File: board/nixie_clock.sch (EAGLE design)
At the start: 43 parts, among them U1 AMS1117-5.0, U2 SN74141N

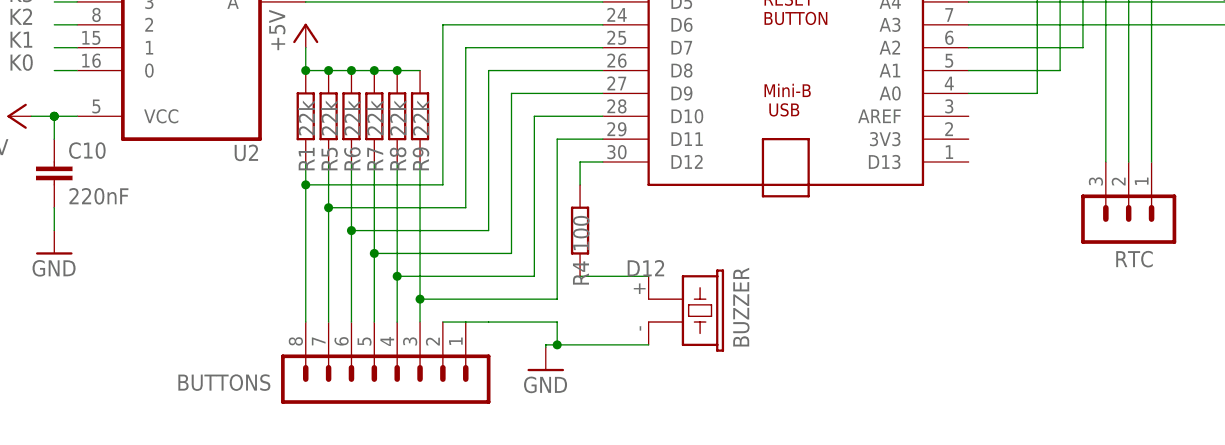
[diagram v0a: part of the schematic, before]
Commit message: added button to D13
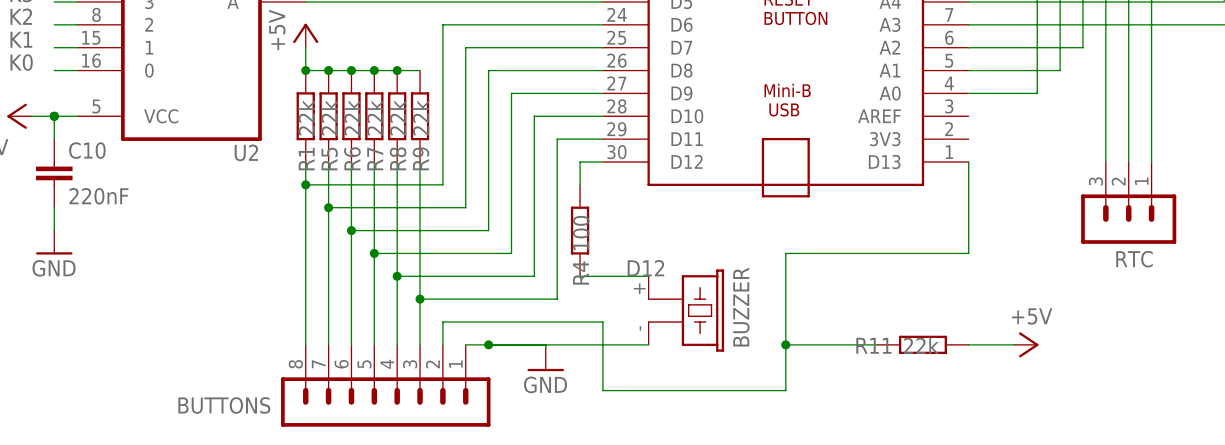
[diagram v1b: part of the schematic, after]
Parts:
- added R11: 22k, rcl:R-EU_0204/7
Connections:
- new net N$4: ARDUINO_NANO1.D13, BUTTONS.2, R11.2
- net +5V: now also R11.1
- net GND: no longer BUTTONS.2
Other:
- moved on the sheet: BUTTONS
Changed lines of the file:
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@@
 <part name="J1" library="con-jack" library_urn="urn:adsk.eagle:library:154" deviceset="DCJ0303" device="" package3d_urn="urn:adsk.eagle:package:7493/1"/>
 <part name="SHNT" library="switch" library_urn="urn:adsk.eagle:library:380" deviceset="320-916" device="" package3d_urn="urn:adsk.eagle:package:27678/1"/>
+<part name="R11" library="rcl" library_urn="urn:adsk.eagle:library:334" deviceset="R-EU_" device="0204/7" package3d_urn="urn:adsk.eagle:package:23498/2" value="22k"/>
+<part name="P+5" library="supply1" library_urn="urn:adsk.eagle:library:371" deviceset="+5V" device=""/>
 </parts>
 <sheets>
@@
 <frame x1="172.72" y1="127" x2="254" y2="177.8" columns="0" rows="1" layer="97" border-left="no" border-top="no" border-right="no" border-bottom="no"/>
 <text x="205.74" y="170.18" size="3.81" layer="97">200V Power supply</text>
-<frame x1="259.08" y1="53.34" x2="477.52" y2="215.9" columns="0" rows="0" layer="97" border-left="no" border-top="no" border-right="no" border-bottom="no"/>
+<frame x1="259.08" y1="45.72" x2="477.52" y2="208.28" columns="0" rows="0" layer="97" border-left="no" border-top="no" border-right="no" border-bottom="no"/>
 <text x="281.94" y="200.66" size="3.81" layer="97">Main circuit</text>
 <text x="45.72" y="114.3" size="3.81" layer="97">Nixie Tubes</text>
@@
 <attribute name="VALUE" x="309.118" y="88.138" size="1.778" layer="96" rot="R270"/>
 </instance>
-<instance part="BUTTONS" gate="1" x="307.34" y="55.88" smashed="yes" rot="R90">
-<attribute name="VALUE" x="320.04" y="54.61" size="1.778" layer="96" rot="R90"/>
-<attribute name="NAME" x="293.37" y="57.658" size="1.778" layer="95" rot="R180"/>
+<instance part="BUTTONS" gate="1" x="307.34" y="53.34" smashed="yes" rot="R90">
+<attribute name="VALUE" x="320.04" y="52.07" size="1.778" layer="96" rot="R90"/>
+<attribute name="NAME" x="293.37" y="55.118" size="1.778" layer="95" rot="R180"/>
 </instance>
 <instance part="BUZZER" gate="G$1" x="337.82" y="66.04" smashed="yes" rot="R270">
@@
 <attribute name="NAME" x="237.49" y="145.415" size="1.778" layer="95" rot="R90"/>
 <attribute name="VALUE" x="240.03" y="149.86" size="1.778" layer="96" rot="R90"/>
+</instance>
+<instance part="R11" gate="G$1" x="365.76" y="60.96" smashed="yes" rot="R180">
+<attribute name="NAME" x="362.458" y="61.7474" size="1.778" layer="95" rot="R180"/>
+<attribute name="VALUE" x="367.538" y="61.722" size="1.778" layer="96" rot="R180"/>
+</instance>
+<instance part="P+5" gate="1" x="378.46" y="60.96" smashed="yes" rot="R270">
+<attribute name="VALUE" x="375.412" y="63.246" size="1.778" layer="96"/>
 </instance>
 </instances>
@@
 <pinref part="BUZZER" gate="G$1" pin="2"/>
 <wire x1="323.85" y1="60.706" x2="323.85" y2="60.96" width="0.1524" layer="91"/>
-<wire x1="323.85" y1="60.96" x2="325.12" y2="60.96" width="0.1524" layer="91"/>
+<wire x1="323.85" y1="60.96" x2="317.5" y2="60.96" width="0.1524" layer="91"/>
 <pinref part="BUTTONS" gate="1" pin="1"/>
-<wire x1="325.12" y1="60.96" x2="335.28" y2="60.96" width="0.1524" layer="91"/>
-<wire x1="314.96" y1="63.5" x2="317.5" y2="63.5" width="0.1524" layer="91"/>
-<wire x1="317.5" y1="63.5" x2="325.12" y2="63.5" width="0.1524" layer="91"/>
-<wire x1="325.12" y1="63.5" x2="325.12" y2="60.96" width="0.1524" layer="91"/>
-<junction x="325.12" y="60.96"/>
-<pinref part="BUTTONS" gate="1" pin="2"/>
-<wire x1="312.42" y1="63.5" x2="314.96" y2="63.5" width="0.1524" layer="91"/>
+<wire x1="317.5" y1="60.96" x2="335.28" y2="60.96" width="0.1524" layer="91"/>
+<wire x1="314.96" y1="60.96" x2="317.5" y2="60.96" width="0.1524" layer="91"/>
+<junction x="317.5" y="60.96"/>
 </segment>
 <segment>
@@
 <pinref part="P+8" gate="1" pin="+5V"/>
 <wire x1="398.78" y1="116.84" x2="398.78" y2="121.92" width="0.1524" layer="91"/>
+</segment>
+<segment>
+<pinref part="P+5" gate="1" pin="+5V"/>
+<pinref part="R11" gate="G$1" pin="1"/>
+<wire x1="375.92" y1="60.96" x2="370.84" y2="60.96" width="0.1524" layer="91"/>
 </segment>
 </net>
@@
 <wire x1="309.88" y1="81.28" x2="309.88" y2="66.04" width="0.1524" layer="91"/>
 <pinref part="ARDUINO_NANO1" gate="G$1" pin="D11"/>
-<wire x1="309.88" y1="66.04" x2="309.88" y2="63.5" width="0.1524" layer="91"/>
+<wire x1="309.88" y1="66.04" x2="309.88" y2="60.96" width="0.1524" layer="91"/>
 <wire x1="330.2" y1="83.82" x2="325.12" y2="83.82" width="0.1524" layer="91"/>
 <wire x1="325.12" y1="83.82" x2="325.12" y2="66.04" width="0.1524" layer="91"/>
@@
 <wire x1="307.34" y1="81.28" x2="307.34" y2="68.58" width="0.1524" layer="91"/>
 <pinref part="ARDUINO_NANO1" gate="G$1" pin="D10"/>
-<wire x1="307.34" y1="68.58" x2="307.34" y2="63.5" width="0.1524" layer="91"/>
+<wire x1="307.34" y1="68.58" x2="307.34" y2="60.96" width="0.1524" layer="91"/>
 <wire x1="330.2" y1="86.36" x2="322.58" y2="86.36" width="0.1524" layer="91"/>
 <wire x1="322.58" y1="86.36" x2="322.58" y2="68.58" width="0.1524" layer="91"/>
@@
 <wire x1="304.8" y1="81.28" x2="304.8" y2="71.12" width="0.1524" layer="91"/>
 <pinref part="ARDUINO_NANO1" gate="G$1" pin="D9"/>
-<wire x1="304.8" y1="71.12" x2="304.8" y2="63.5" width="0.1524" layer="91"/>
+<wire x1="304.8" y1="71.12" x2="304.8" y2="60.96" width="0.1524" layer="91"/>
 <wire x1="330.2" y1="88.9" x2="320.04" y2="88.9" width="0.1524" layer="91"/>
 <wire x1="320.04" y1="88.9" x2="320.04" y2="71.12" width="0.1524" layer="91"/>
@@
 <wire x1="302.26" y1="81.28" x2="302.26" y2="73.66" width="0.1524" layer="91"/>
 <pinref part="ARDUINO_NANO1" gate="G$1" pin="D8"/>
-<wire x1="302.26" y1="73.66" x2="302.26" y2="63.5" width="0.1524" layer="91"/>
+<wire x1="302.26" y1="73.66" x2="302.26" y2="60.96" width="0.1524" layer="91"/>
 <wire x1="330.2" y1="91.44" x2="317.5" y2="91.44" width="0.1524" layer="91"/>
 <wire x1="317.5" y1="91.44" x2="317.5" y2="73.66" width="0.1524" layer="91"/>
@@
 <wire x1="299.72" y1="81.28" x2="299.72" y2="76.2" width="0.1524" layer="91"/>
 <pinref part="ARDUINO_NANO1" gate="G$1" pin="D7"/>
-<wire x1="299.72" y1="76.2" x2="299.72" y2="63.5" width="0.1524" layer="91"/>
+<wire x1="299.72" y1="76.2" x2="299.72" y2="60.96" width="0.1524" layer="91"/>
 <wire x1="330.2" y1="93.98" x2="314.96" y2="93.98" width="0.1524" layer="91"/>
 <wire x1="314.96" y1="93.98" x2="314.96" y2="76.2" width="0.1524" layer="91"/>
@@
 <wire x1="297.18" y1="81.28" x2="297.18" y2="78.74" width="0.1524" layer="91"/>
 <pinref part="ARDUINO_NANO1" gate="G$1" pin="D6"/>
-<wire x1="297.18" y1="78.74" x2="297.18" y2="63.5" width="0.1524" layer="91"/>
+<wire x1="297.18" y1="78.74" x2="297.18" y2="60.96" width="0.1524" layer="91"/>
 <wire x1="330.2" y1="96.52" x2="312.42" y2="96.52" width="0.1524" layer="91"/>
 <wire x1="312.42" y1="96.52" x2="312.42" y2="78.74" width="0.1524" layer="91"/>
@@
 </segment>
 </net>
+<net name="N$4" class="0">
+<segment>
+<pinref part="R11" gate="G$1" pin="2"/>
+<wire x1="360.68" y1="60.96" x2="350.52" y2="60.96" width="0.1524" layer="91"/>
+<wire x1="350.52" y1="60.96" x2="350.52" y2="55.88" width="0.1524" layer="91"/>
+<wire x1="350.52" y1="55.88" x2="330.2" y2="55.88" width="0.1524" layer="91"/>
+<wire x1="330.2" y1="55.88" x2="330.2" y2="63.5" width="0.1524" layer="91"/>
+<pinref part="BUTTONS" gate="1" pin="2"/>
+<wire x1="330.2" y1="63.5" x2="312.42" y2="63.5" width="0.1524" layer="91"/>
+<wire x1="312.42" y1="63.5" x2="312.42" y2="60.96" width="0.1524" layer="91"/>
+<pinref part="ARDUINO_NANO1" gate="G$1" pin="D13"/>
+<wire x1="370.84" y1="81.28" x2="370.84" y2="71.12" width="0.1524" layer="91"/>
+<wire x1="370.84" y1="71.12" x2="350.52" y2="71.12" width="0.1524" layer="91"/>
+<wire x1="350.52" y1="71.12" x2="350.52" y2="60.96" width="0.1524" layer="91"/>
+<junction x="350.52" y="60.96"/>
+</segment>
+</net>

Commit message: finalized board component layout
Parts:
- removed J1: (no value), con-jack:DCJ0303
- added INPUT: 22-23-2021, con-molex:22-23-2021
- SHNT: value (none) -> 22-23-2021; device switch:320-916 -> con-molex:22-23-2021
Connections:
- net +12V: now also SHNT-2.S; no longer SHNT.O, SHNT.S
- net GND: now also INPUT-2.S, SHNT-1.S; no longer J1.1, J1.2, SHNT.P
- net N$1: now also INPUT-1.S; no longer J1.3
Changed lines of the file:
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@@
 <part name="R10" library="rcl" library_urn="urn:adsk.eagle:library:334" deviceset="R-EU_" device="0204/7" package3d_urn="urn:adsk.eagle:package:23498/2" value="670"/>
 <part name="GND9" library="supply1" library_urn="urn:adsk.eagle:library:371" deviceset="GND" device=""/>
-<part name="J1" library="con-jack" library_urn="urn:adsk.eagle:library:154" deviceset="DCJ0303" device="" package3d_urn="urn:adsk.eagle:package:7493/1"/>
-<part name="SHNT" library="switch" library_urn="urn:adsk.eagle:library:380" deviceset="320-916" device="" package3d_urn="urn:adsk.eagle:package:27678/1"/>
 <part name="R11" library="rcl" library_urn="urn:adsk.eagle:library:334" deviceset="R-EU_" device="0204/7" package3d_urn="urn:adsk.eagle:package:23498/2" value="22k"/>
 <part name="P+5" library="supply1" library_urn="urn:adsk.eagle:library:371" deviceset="+5V" device=""/>
+<part name="SHNT" library="con-molex" library_urn="urn:adsk.eagle:library:165" deviceset="22-23-2021" device="" package3d_urn="urn:adsk.eagle:package:8078633/1"/>
+<part name="INPUT" library="con-molex" library_urn="urn:adsk.eagle:library:165" deviceset="22-23-2021" device="" package3d_urn="urn:adsk.eagle:package:8078633/1"/>
 </parts>
 <sheets>
@@
 <attribute name="VALUE" x="269.24" y="157.48" size="1.778" layer="96"/>
 </instance>
-<instance part="J1" gate="G$1" x="45.72" y="167.64" smashed="yes">
-<attribute name="NAME" x="43.18" y="171.45" size="1.778" layer="95"/>
-<attribute name="VALUE" x="43.18" y="161.29" size="1.778" layer="96"/>
-</instance>
-<instance part="SHNT" gate="1" x="243.84" y="147.32" smashed="yes">
-<attribute name="NAME" x="237.49" y="145.415" size="1.778" layer="95" rot="R90"/>
-<attribute name="VALUE" x="240.03" y="149.86" size="1.778" layer="96" rot="R90"/>
-</instance>
 <instance part="R11" gate="G$1" x="365.76" y="60.96" smashed="yes" rot="R180">
 <attribute name="NAME" x="362.458" y="61.7474" size="1.778" layer="95" rot="R180"/>
@@
 <instance part="P+5" gate="1" x="378.46" y="60.96" smashed="yes" rot="R270">
 <attribute name="VALUE" x="375.412" y="63.246" size="1.778" layer="96"/>
+</instance>
+<instance part="SHNT" gate="-1" x="243.84" y="142.24" smashed="yes">
+<attribute name="NAME" x="246.38" y="141.478" size="1.524" layer="95"/>
+</instance>
+<instance part="SHNT" gate="-2" x="243.84" y="144.78" smashed="yes">
+<attribute name="NAME" x="246.38" y="144.018" size="1.524" layer="95"/>
+</instance>
+<instance part="INPUT" gate="-1" x="48.26" y="167.64" smashed="yes" rot="R180">
+<attribute name="NAME" x="50.8" y="170.942" size="1.524" layer="95" rot="R180"/>
+</instance>
+<instance part="INPUT" gate="-2" x="48.26" y="165.1" smashed="yes" rot="R180">
+<attribute name="NAME" x="50.8" y="163.322" size="1.524" layer="95" rot="R180"/>
 </instance>
 </instances>
@@
 <segment>
 <pinref part="GND1" gate="1" pin="GND"/>
-<wire x1="58.42" y1="142.24" x2="73.66" y2="142.24" width="0.1524" layer="91"/>
+<wire x1="55.88" y1="142.24" x2="73.66" y2="142.24" width="0.1524" layer="91"/>
 <pinref part="C1" gate="G$1" pin="2"/>
 <wire x1="73.66" y1="142.24" x2="91.44" y2="142.24" width="0.1524" layer="91"/>
@@
 <wire x1="101.6" y1="147.32" x2="101.6" y2="142.24" width="0.1524" layer="91"/>
 <junction x="101.6" y="142.24"/>
-<wire x1="58.42" y1="142.24" x2="58.42" y2="167.64" width="0.1524" layer="91"/>
-<pinref part="J1" gate="G$1" pin="2"/>
-<wire x1="58.42" y1="167.64" x2="53.34" y2="167.64" width="0.1524" layer="91"/>
-<pinref part="J1" gate="G$1" pin="1"/>
-<wire x1="53.34" y1="170.18" x2="58.42" y2="170.18" width="0.1524" layer="91"/>
-<wire x1="58.42" y1="170.18" x2="58.42" y2="167.64" width="0.1524" layer="91"/>
-<junction x="58.42" y="167.64"/>
+<wire x1="55.88" y1="142.24" x2="55.88" y2="165.1" width="0.1524" layer="91"/>
+<pinref part="INPUT" gate="-2" pin="S"/>
+<wire x1="55.88" y1="165.1" x2="50.8" y2="165.1" width="0.1524" layer="91"/>
 </segment>
 <segment>
@@
 <wire x1="203.2" y1="139.7" x2="203.2" y2="137.16" width="0.1524" layer="91"/>
 <junction x="203.2" y="137.16"/>
+<label x="187.96" y="147.32" size="1.778" layer="95"/>
+<pinref part="SHNT" gate="-1" pin="S"/>
+<wire x1="241.3" y1="142.24" x2="241.3" y2="137.16" width="0.1524" layer="91"/>
+<wire x1="241.3" y1="137.16" x2="226.06" y2="137.16" width="0.1524" layer="91"/>
 <junction x="226.06" y="137.16"/>
-<label x="187.96" y="147.32" size="1.778" layer="95"/>
-<wire x1="226.06" y1="137.16" x2="246.38" y2="137.16" width="0.1524" layer="91"/>
-<pinref part="SHNT" gate="1" pin="P"/>
-<wire x1="246.38" y1="137.16" x2="246.38" y2="142.24" width="0.1524" layer="91"/>
 </segment>
 <segment>
@@
 <wire x1="226.06" y1="147.32" x2="226.06" y2="152.4" width="0.1524" layer="91"/>
 <junction x="226.06" y="152.4"/>
-<wire x1="243.84" y1="157.48" x2="226.06" y2="157.48" width="0.1524" layer="91"/>
 <junction x="226.06" y="157.48"/>
-<pinref part="SHNT" gate="1" pin="O"/>
-<wire x1="243.84" y1="152.4" x2="243.84" y2="157.48" width="0.1524" layer="91"/>
-<pinref part="SHNT" gate="1" pin="S"/>
-<wire x1="248.92" y1="152.4" x2="248.92" y2="157.48" width="0.1524" layer="91"/>
-<wire x1="248.92" y1="157.48" x2="243.84" y2="157.48" width="0.1524" layer="91"/>
-<junction x="243.84" y="157.48"/>
+<pinref part="SHNT" gate="-2" pin="S"/>
+<wire x1="241.3" y1="157.48" x2="226.06" y2="157.48" width="0.1524" layer="91"/>
+<wire x1="241.3" y1="157.48" x2="241.3" y2="144.78" width="0.1524" layer="91"/>
 </segment>
 </net>
@@
 <net name="N$1" class="0">
 <segment>
-<pinref part="J1" gate="G$1" pin="3"/>
-<wire x1="53.34" y1="165.1" x2="60.96" y2="165.1" width="0.1524" layer="91"/>
-<wire x1="60.96" y1="165.1" x2="60.96" y2="167.64" width="0.1524" layer="91"/>
 <pinref part="D1" gate="G$1" pin="A"/>
-<wire x1="60.96" y1="167.64" x2="63.5" y2="167.64" width="0.1524" layer="91"/>
-</segment>
-</net>
+<pinref part="INPUT" gate="-1" pin="S"/>
+<wire x1="63.5" y1="167.64" x2="50.8" y2="167.64" width="0.1524" layer="91"/>
+</segment>
+</net>

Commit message: PCB redesign
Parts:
- removed INPUT, SHNT: 22-23-2021, con-molex:22-23-2021
- removed OK1, OK2, OK3, OK4, OK5: SFH618A-5X007, optocoupler:SFH618A-5X007
- removed R11, R6, R7, R8, R9: 22k, rcl:R-EU_0204/7
- added 10H, 10MIN, 1H, 1MIN, DOT: PC-TLP127, we-opto:PC-TLP127
- added 12V: TERMINAL_2P, KF301-2P-Terminal:TERMINAL_2P
- added 12V_INPUT: DCJ0202, con-jack:DCJ0202
- 200V: value (none) -> TERMINAL_2P; device con-amp-quick:M03 -> KF301-2P-Terminal:TERMINAL_2P
- R10: value 670 -> 56k
- RTC: device con-lstb:MA03-1 -> con-lstb:MA05-1
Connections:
- removed net N$1: D1.A, INPUT-1.S
- removed net N$21: ARDUINO_NANO1.D6, BUTTONS.8, R1.2
- removed net N$22: ARDUINO_NANO1.A6, RTC.2
- removed net N$23: ARDUINO_NANO1.A7, RTC.1
- new net N$3: ARDUINO_NANO1.D8, RTC.1
- new net N$7: ARDUINO_NANO1.D6, RTC.3
- net +12V: no longer SHNT-2.S
- net +5V: now also R1.2, R5.2, RTC.5; no longer ARDUINO_NANO1.5V, R1.1, R11.1, R5.1, R6.1, R7.1, R8.1, R9.1
- net 12V: now also 12V.2, 12V_INPUT.1, D1.A; no longer 200V.2
- net 200V: now also 200V.2; no longer 200V.3
- net A_10H: now also 10H.TE; no longer OK1.EMIT
- net A_10MIN: now also 10MIN.TE; no longer OK4.EMIT
- net A_1H: now also 1H.TE; no longer OK2.EMIT
- net A_1MIN: now also 1MIN.TE; no longer OK5.EMIT
- net A_DOT: now also DOT.TE; no longer OK3.EMIT
- net GND: now also 12V.1, 12V_INPUT.2, 12V_INPUT.3, BUTTONS.2, RTC.4; no longer INPUT-2.S, SHNT-1.S
- net N$10: now also ARDUINO_NANO1.A7, R1.1; no longer ARDUINO_NANO1.D11, R9.2
- net N$15: now also 10H.A; no longer OK1.A
- net N$16: now also 10H.C, 10MIN.C, 1H.C, 1MIN.C, DOT.C; no longer OK1.C, OK2.C, OK3.C, OK4.C, OK5.C
- net N$17: now also ARDUINO_NANO1.A5, BUTTONS.5; no longer ARDUINO_NANO1.D10, BUTTONS.4, R8.2
- net N$18: now also ARDUINO_NANO1.D11, BUTTONS.6; no longer ARDUINO_NANO1.D9, BUTTONS.5, R7.2
- net N$19: now also ARDUINO_NANO1.D10, BUTTONS.7; no longer ARDUINO_NANO1.D8, BUTTONS.6, R6.2
- net N$20: now also ARDUINO_NANO1.D9, BUTTONS.8; no longer ARDUINO_NANO1.D7, BUTTONS.7, R5.2
- net N$26: now also 1H.A; no longer OK2.A
- net N$27: now also DOT.A; no longer OK3.A
- net N$28: now also 10MIN.A; no longer OK4.A
- net N$29: now also 1MIN.A; no longer OK5.A
- net N$4: now also ARDUINO_NANO1.D7, RTC.2; no longer ARDUINO_NANO1.D13, BUTTONS.2, R11.2
- net N$5: now also 10H.TC, 10MIN.TC, 1H.TC, 1MIN.TC, DOT.TC; no longer OK1.COL, OK2.COL, OK3.COL, OK4.COL, OK5.COL
- net N$9: now also ARDUINO_NANO1.A6, BUTTONS.4, R5.1; no longer ARDUINO_NANO1.A5, RTC.3
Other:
- moved on the sheet: BUTTONS, BUZZER, L2, R1, R3, R4, R5
